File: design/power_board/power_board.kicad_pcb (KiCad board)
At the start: 2 copper layers, 68.5 x 38.5 mm, 33 parts, among them J1 Screw_Terminal_01x02, J2 Screw_Terminal_01x02, J3 Screw_Terminal_01x03, U1 LV2862YDDCR, U3 LM317MDCYR

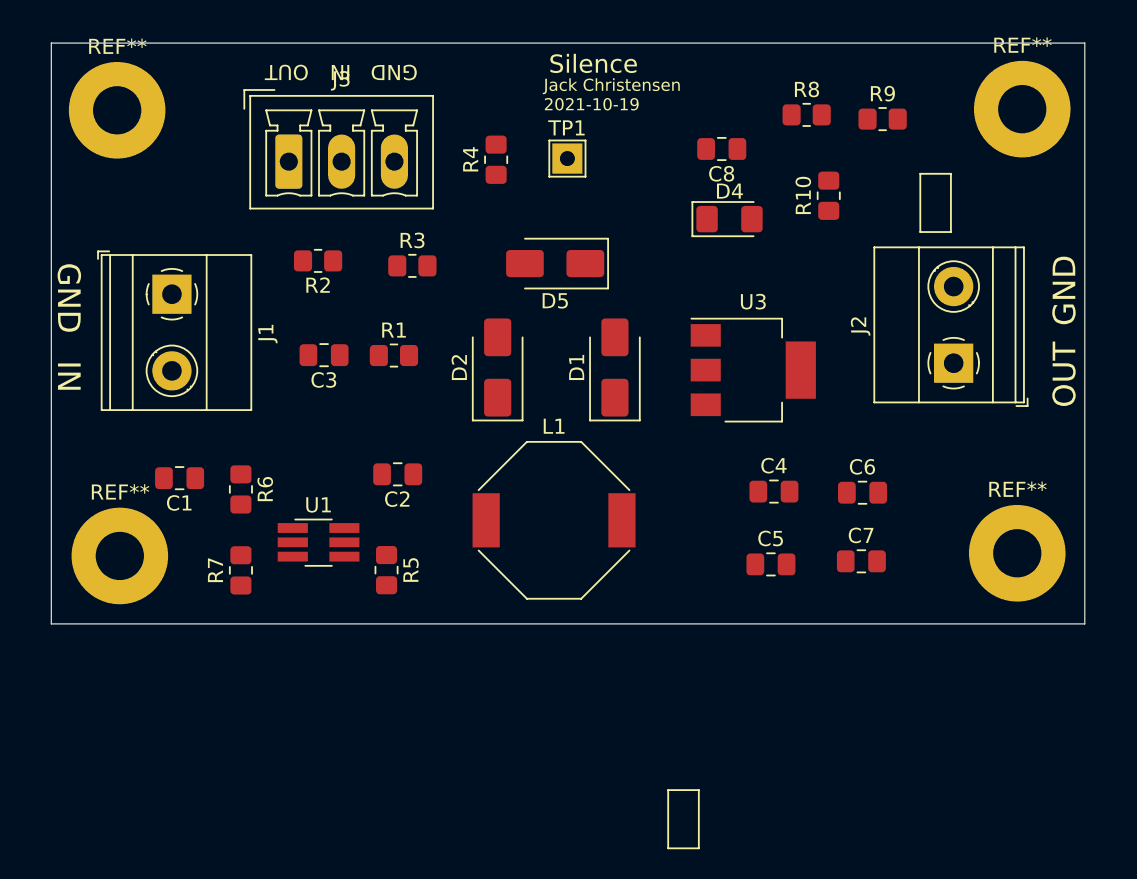
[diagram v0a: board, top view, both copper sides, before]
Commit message: rounded corners
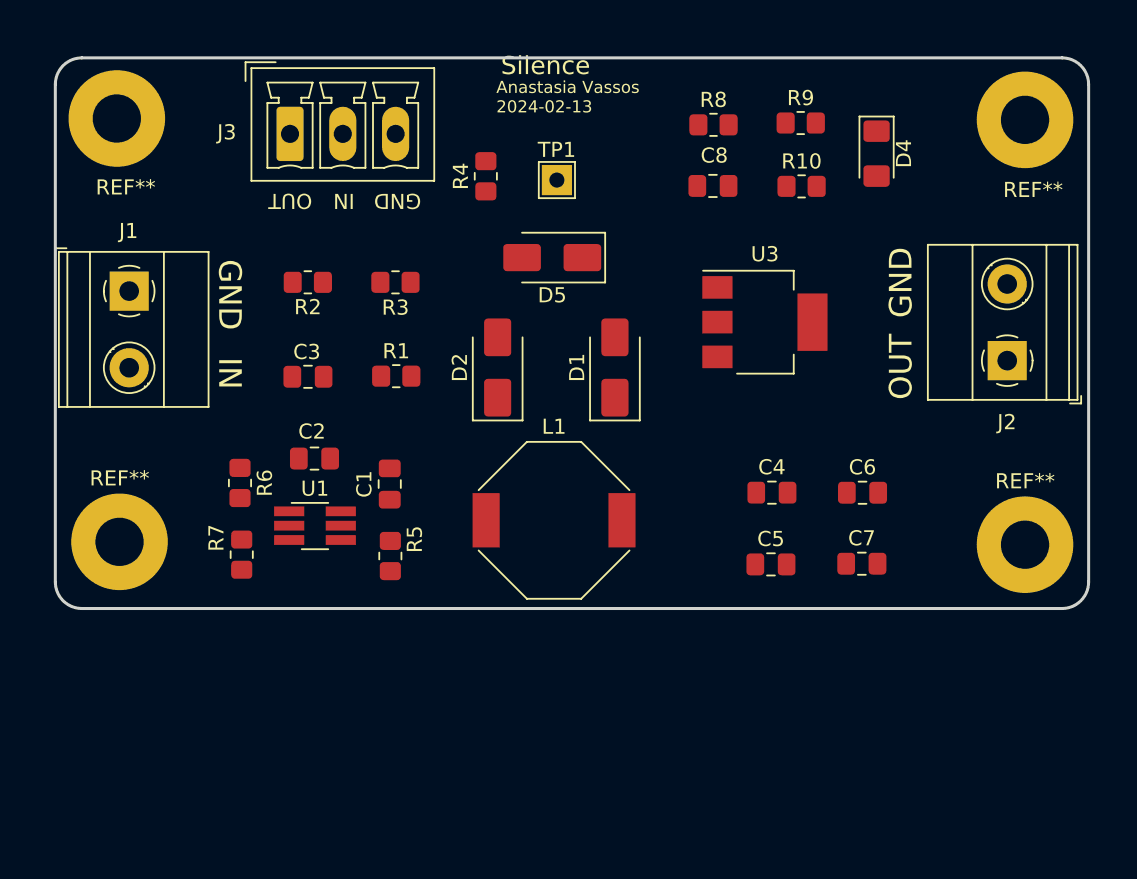
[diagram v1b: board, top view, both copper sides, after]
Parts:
- moved C1 13.9 mm to (125.2, 117.2), turned to 90 degrees
- moved D4 10.7 mm to (157.4, 95.3), turned to -90 degrees
- moved R8 6.21 mm to (146.6, 93.4)
- moved C2 5.61 mm to (120.2, 115.5)
- moved R9 5.44 mm to (152.4, 93.3)
- moved J2 3.55 mm to (166.1, 109.0)
- moved U3 3.27 mm to (150.1, 106.5)
- moved J1 2.84 mm to (107.9, 104.4)
- moved C8 2.52 mm to (146.6, 97.5)
- moved R10 1.90 mm to (152.5, 97.5), turned to 0 degrees
- moved J3 1.84 mm to (118.6, 94.0)
- moved C3 1.79 mm to (119.8, 110.1)
- moved TP1 1.58 mm to (136.3, 97.1)
- moved R2 1.57 mm to (119.8, 103.9)
- moved R3 1.56 mm to (125.6, 103.9)
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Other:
- board size 68.5 x 38.5 mm -> 68.5 x 36.5 mm
- board text added: "Anastasia Vassos 2024-02-13"
- board text removed: "Jack Christensen 2021-10-19"

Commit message: Moved capacitors up
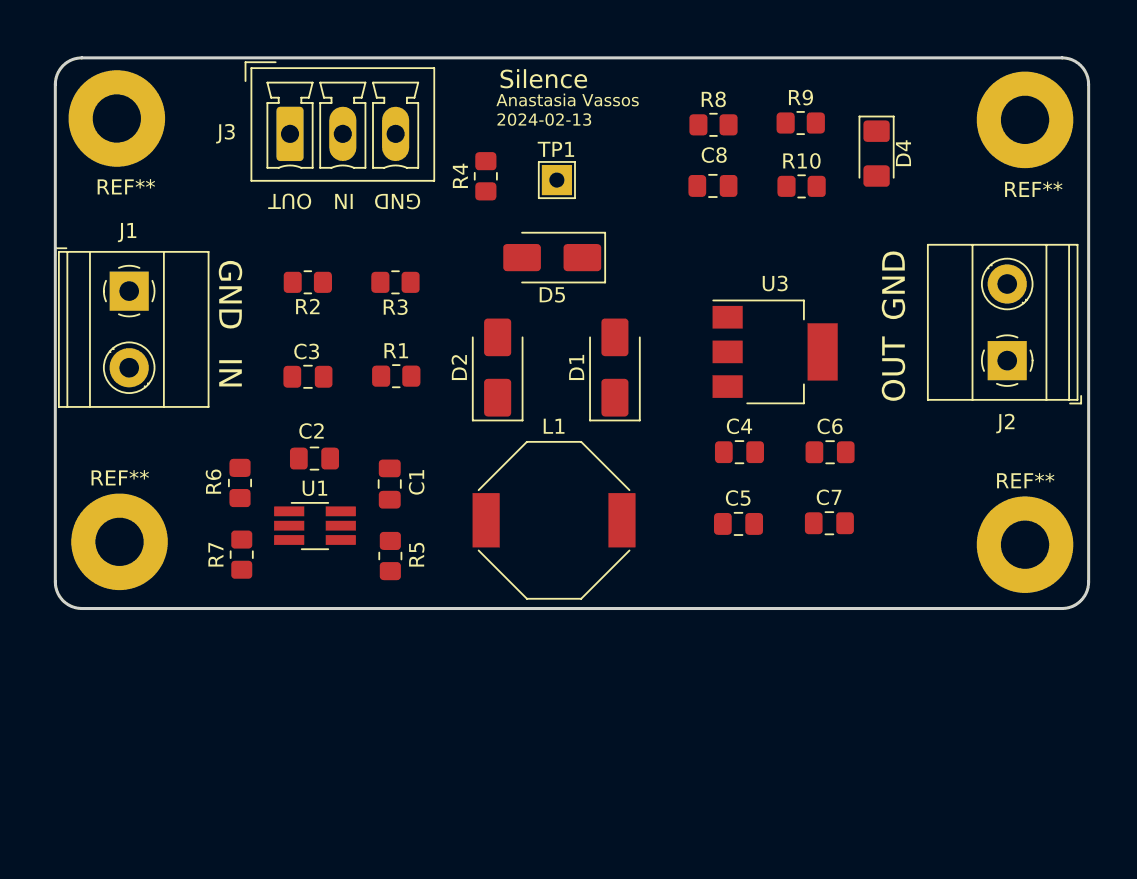
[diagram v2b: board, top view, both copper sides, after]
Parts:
- moved C5 3.44 mm to (148.3, 119.9)
- moved C6 3.44 mm to (154.4, 115.1)
- moved C7 3.44 mm to (154.3, 119.8)
- moved C4 3.44 mm to (148.4, 115.1)
- moved U3 2.08 mm to (150.7, 108.5)
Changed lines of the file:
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@@
     (property "ki_keywords" "R res resistor")
     (attr smd)
-    (fp_text reference "R7" (at 1.11 -1.675 90) (layer "F.SilkS")
+    (fp_text reference "R7" (at -0.01 -1.675 90) (layer "F.SilkS")
         (effects (font (size 1 1) (thickness 0.15)))
     )
@@
   )
   (footprint "Capacitor_SMD:C_0805_2012Metric_Pad1.18x1.45mm_HandSolder" (layer "F.Cu")
-    (at 156.4725 122.51)
+    (at 154.3225 119.828)
     (descr "Capacitor SMD 0805 (2012 Metric), square (rectangular) end terminal, IPC_7351 nominal with elongated pad for handsoldering. (Body size source: IPC-SM-782 page 76, https://www.pcb-3d.com/wordpress/wp-content/uploads/ipc-sm-782a_amendment_1_and_2.pdf, https://docs.google.com/spreadsheets/d/1BsfQQcO9C6DZCsRaXUlFlo91Tg2WpOkGARC1WS5S8t0/edit?usp=sharing), generated with kicad-footprint-generator")
     (tags "capacitor handsolder")
@@
   )
   (footprint "Capacitor_SMD:C_0805_2012Metric_Pad1.18x1.45mm_HandSolder" (layer "F.Cu")
-    (at 156.5187 117.8052)
+    (at 154.3687 115.1232)
     (descr "Capacitor SMD 0805 (2012 Metric), square (rectangular) end terminal, IPC_7351 nominal with elongated pad for handsoldering. (Body size source: IPC-SM-782 page 76, https://www.pcb-3d.com/wordpress/wp-content/uploads/ipc-sm-782a_amendment_1_and_2.pdf, https://docs.google.com/spreadsheets/d/1BsfQQcO9C6DZCsRaXUlFlo91Tg2WpOkGARC1WS5S8t0/edit?usp=sharing), generated with kicad-footprint-generator")
     (tags "capacitor handsolder")
@@
     (property "ki_keywords" "cap capacitor")
     (attr smd)
-    (fp_text reference "C1" (at 0 -1.68 90) (layer "F.SilkS")
+    (fp_text reference "C1" (at 0.136 1.82 90) (layer "F.SilkS")
         (effects (font (size 1 1) (thickness 0.15)))
     )
@@
   )
   (footprint "Capacitor_SMD:C_0805_2012Metric_Pad1.18x1.45mm_HandSolder" (layer "F.Cu")
-    (at 150.4481 122.555)
+    (at 148.2981 119.873)
     (descr "Capacitor SMD 0805 (2012 Metric), square (rectangular) end terminal, IPC_7351 nominal with elongated pad for handsoldering. (Body size source: IPC-SM-782 page 76, https://www.pcb-3d.com/wordpress/wp-content/uploads/ipc-sm-782a_amendment_1_and_2.pdf, https://docs.google.com/spreadsheets/d/1BsfQQcO9C6DZCsRaXUlFlo91Tg2WpOkGARC1WS5S8t0/edit?usp=sharing), generated with kicad-footprint-generator")
     (tags "capacitor handsolder")
@@
     (property "ki_keywords" "R res resistor")
     (attr smd)
-    (fp_text reference "R5" (at -1.11 -1.625 90) (layer "F.SilkS")
+    (fp_text reference "R5" (at -0.08 -1.78 90) (layer "F.SilkS")
         (effects (font (size 1 1) (thickness 0.15)))
     )
@@
   )
   (footprint "Capacitor_SMD:C_0805_2012Metric_Pad1.18x1.45mm_HandSolder" (layer "F.Cu")
-    (at 150.5125 117.8)
+    (at 148.3625 115.118)
     (descr "Capacitor SMD 0805 (2012 Metric), square (rectangular) end terminal, IPC_7351 nominal with elongated pad for handsoldering. (Body size source: IPC-SM-782 page 76, https://www.pcb-3d.com/wordpress/wp-content/uploads/ipc-sm-782a_amendment_1_and_2.pdf, https://docs.google.com/spreadsheets/d/1BsfQQcO9C6DZCsRaXUlFlo91Tg2WpOkGARC1WS5S8t0/edit?usp=sharing), generated with kicad-footprint-generator")
     (tags "capacitor handsolder")
@@
     (property "ki_keywords" "R res resistor")
     (attr smd)
-    (fp_text reference "R6" (at 0 -1.65 90) (layer "F.SilkS")
+    (fp_text reference "R6" (at -0.066 1.717 90) (layer "F.SilkS")
         (effects (font (size 1 1) (thickness 0.15)))
     )
@@
   )
   (footprint "Package_TO_SOT_SMD:SOT-223-3_TabPin2" (layer "F.Cu")
-    (at 150.05 106.5)
+    (at 150.724 108.472)
     (descr "module CMS SOT223 4 pins")
     (tags "CMS SOT")
@@
   (gr_arc (start 169.746712 88.98) (mid 170.990703 89.495304) (end 171.506024 90.739312)
     (stroke (width 0.2) (type solid)) (layer "Edge.Cuts"))
-  (gr_text "GND" (at 159.07 103.872 90) (layer "F.SilkS")
+  (gr_text "GND" (at 158.626 104.052 90) (layer "F.SilkS")
     (effects (font (size 1.5 1.5) (thickness 0.25)))
   )
@@
     (effects (font (size 1 1) (thickness 0.15)))
   )
-  (gr_text "Silence" (at 135.51 89.5) (layer "F.SilkS")
+  (gr_text "Silence" (at 135.382 90.424) (layer "F.SilkS")
     (effects (font (size 1.2 1.2) (thickness 0.2)))
   )
-  (gr_text "OUT" (at 159.07 109.46 90) (layer "F.SilkS")
+  (gr_text "OUT" (at 158.626 109.64 90) (layer "F.SilkS")
     (effects (font (size 1.5 1.5) (thickness 0.25)))
   )
@@
     (effects (font (size 1 1) (thickness 0.15)))
   )
-  (gr_text "Anastasia Vassos\n2024-02-13" (at 132.242 91.58) (layer "F.SilkS")
+  (gr_text "Anastasia Vassos\n2024-02-13" (at 132.242 92.456) (layer "F.SilkS")
     (effects (font (size 0.8 0.8) (thickness 0.12)) (justify left))
   )

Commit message: changed name of board
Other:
- board text added: "DAQ Power"
- board text removed: "Silence"
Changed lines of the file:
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@@
     (effects (font (size 1 1) (thickness 0.15)))
   )
-  (gr_text "Silence" (at 135.382 90.424) (layer "F.SilkS")
+  (gr_text "DAQ Power\n" (at 136.906 90.424) (layer "F.SilkS")
     (effects (font (size 1.2 1.2) (thickness 0.2)))
   )

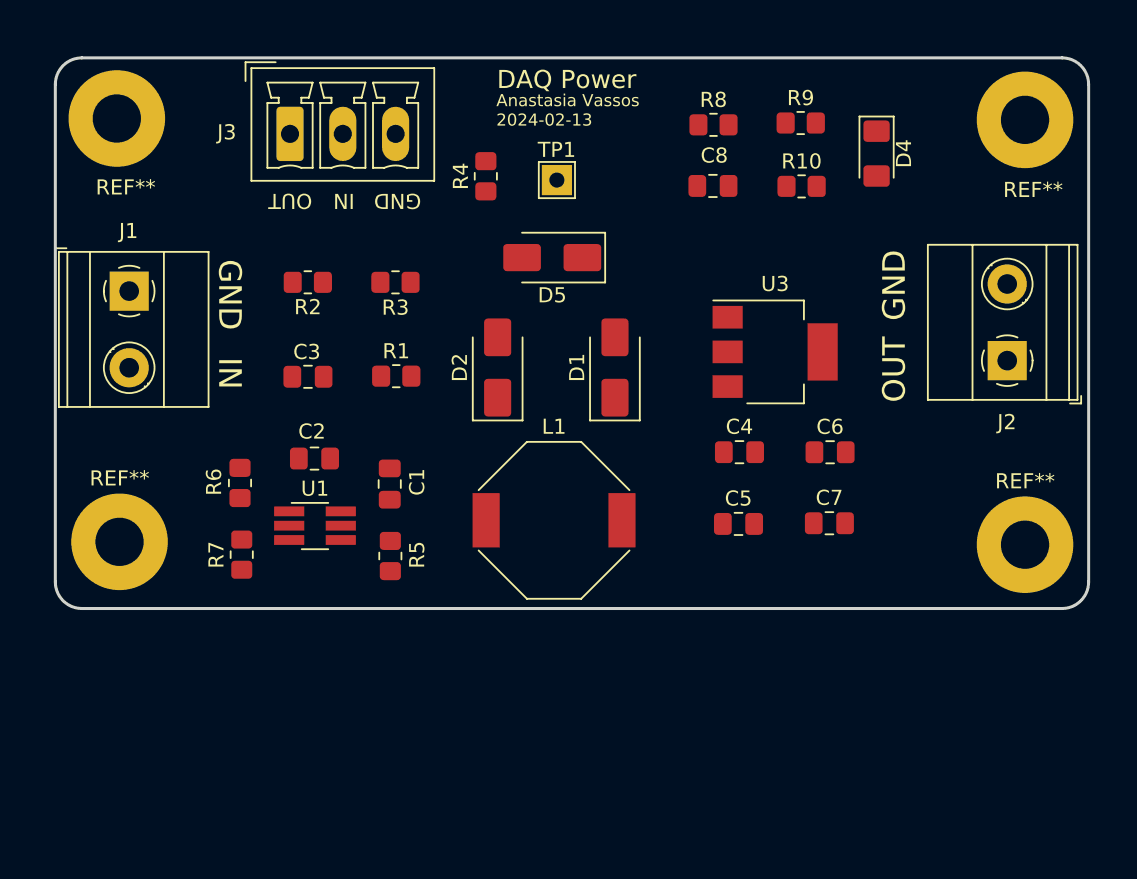
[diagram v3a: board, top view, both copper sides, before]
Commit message: Added logo and aligned J2 and J1
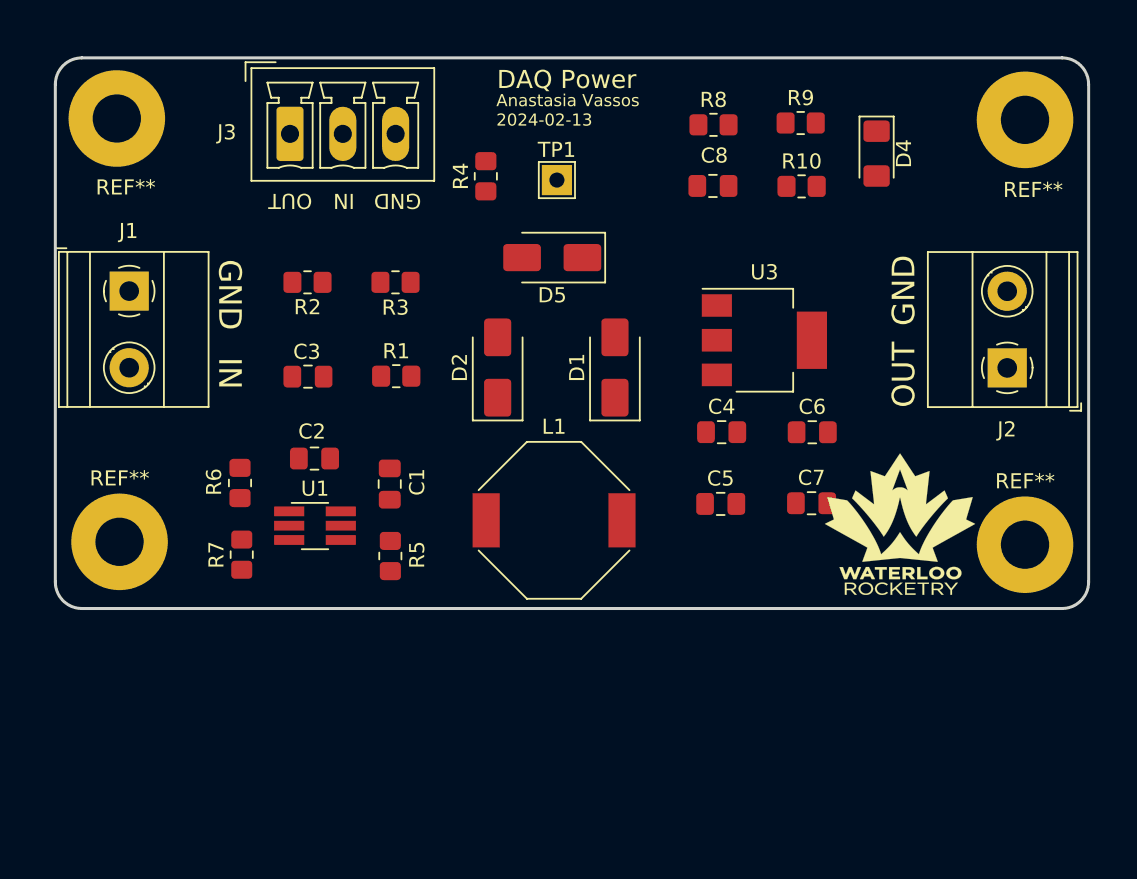
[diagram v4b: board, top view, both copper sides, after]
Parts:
- added G***: LOGO, rlcs:rocketry_logo_small, F.Cu at (159.0, 119.9)
- moved C5 1.78 mm to (147.1, 118.5)
- moved C4 1.78 mm to (147.2, 113.8)
- moved C7 1.78 mm to (153.1, 118.5)
- moved C6 1.78 mm to (153.2, 113.8)
- moved U3 1.05 mm to (150.0, 107.7)
- moved J2 0.48 mm to (166.1, 109.5)

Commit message: routing
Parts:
- moved J1 0.30 mm to (108.2, 104.4)
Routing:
- net +OUT: track 0.00 -> 77.4 mm
- net /buck/VOUT: track 0.00 -> 70.1 mm, vias 0 -> 2
- net +BATT: track 0.00 -> 32.6 mm, vias 0 -> 4
- net Net-(J3-Pin_2): track 0.00 -> 31.4 mm, vias 0 -> 2
- net Net-(D1-A): track 0.00 -> 28.2 mm
- net Net-(D2-K): track 0.00 -> 22.1 mm
- net Net-(J3-Pin_1): track 0.00 -> 21.1 mm
- net Net-(U1-FB): track 0.00 -> 9.58 mm
- net Net-(U1-SHDN_N): track 0.00 -> 5.02 mm
- net Net-(D4-A): track 0.00 -> 4.25 mm
- net Net-(U1-CB): track 0.00 -> 3.77 mm
- added copper zone on B.Cu, net +BATT
- added copper zone on F.Cu, net GND
